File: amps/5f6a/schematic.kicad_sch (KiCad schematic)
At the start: 60 parts, among them T3 2R sec

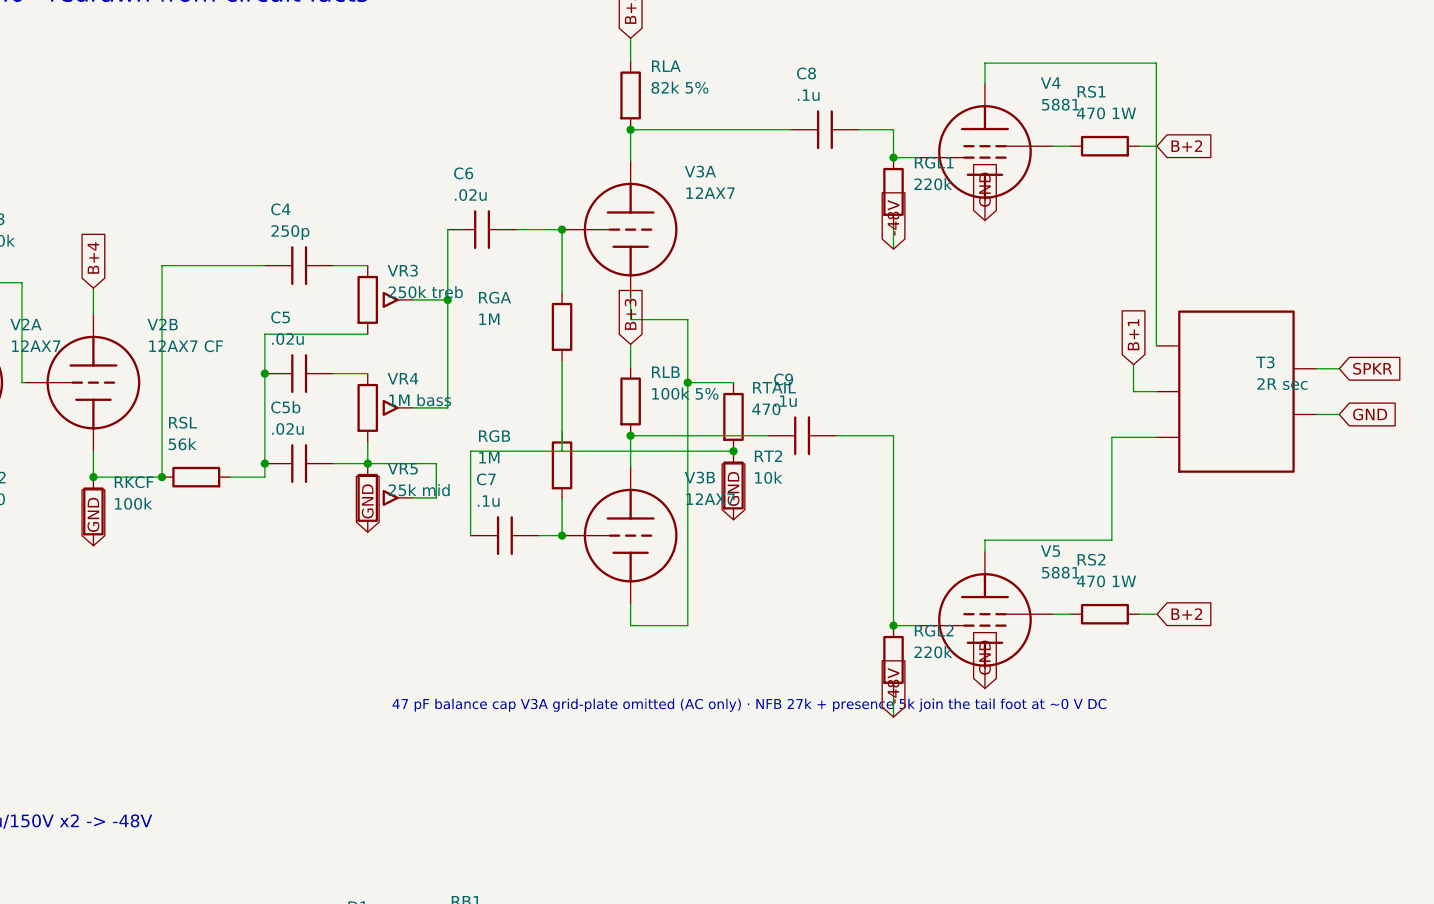
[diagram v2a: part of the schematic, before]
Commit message: Fix: the 5F6-A, AB763 and AA1164 draw the ladder their own sheets print
The tone-stack audit (dc65fcf) flagged these schematics as still drawing
the "canonical FMV" joined network. Fetching each amp's published drawing
and reading it at lug level (300-400 dpi crops) settles all three:

- Fender 5F6-A (I-EG), schematic AND factory layout: the same ladder as
  the 5F6 — 250 pF and the 56k slope both leave the cathode-follower
  node; the first 0.02 uF lands on the node shared by the treble pot's
  LOWER lug and the bass pot; the bass pot is a rheostat (the layout
  sheet straps its wiper into the treble-lug node); the second 0.02 uF
  feeds the MIDDLE POT'S WIPER; the output is the treble wiper alone.
  Unlike the 5F6, the middle pot's foot grounds directly — the presence
  control lives at the phase-inverter tail, as already drawn.

- Fender AB763 (C-FD): BOTH channels print the AA964's two-knob ladder,
  part for part. The vibrato channel's drawn stack was wrong beyond the
  wiring: it was missing its 100k slope and its 0.1/0.047 capacitors
  outright (the 6.8k bleed stood in as a "slope"), and its 47 pF bright
  cap sits across the VOLUME pot (top lug to wiper), not the treble pot.
  The missing parts join bom.yaml (RSV, CBV, CBV2) and the schematic.

- Fender AA1164 (D 045427 rev A): the same two-knob ladder — treble
  lower lug on the far side of the 0.1 uF, bass rheostat above the
  0.047/6.8k foot, treble-wiper output.

The three lab presets now declare `wiring: 'ladder'` and
check_tonestack_wiring asserts the drawn node set for each. All 18
schematics round-trip; the wiring gate reports 9/9.

Co-Authored-By: Claude Fable 5 <noreply@anthropic.com>
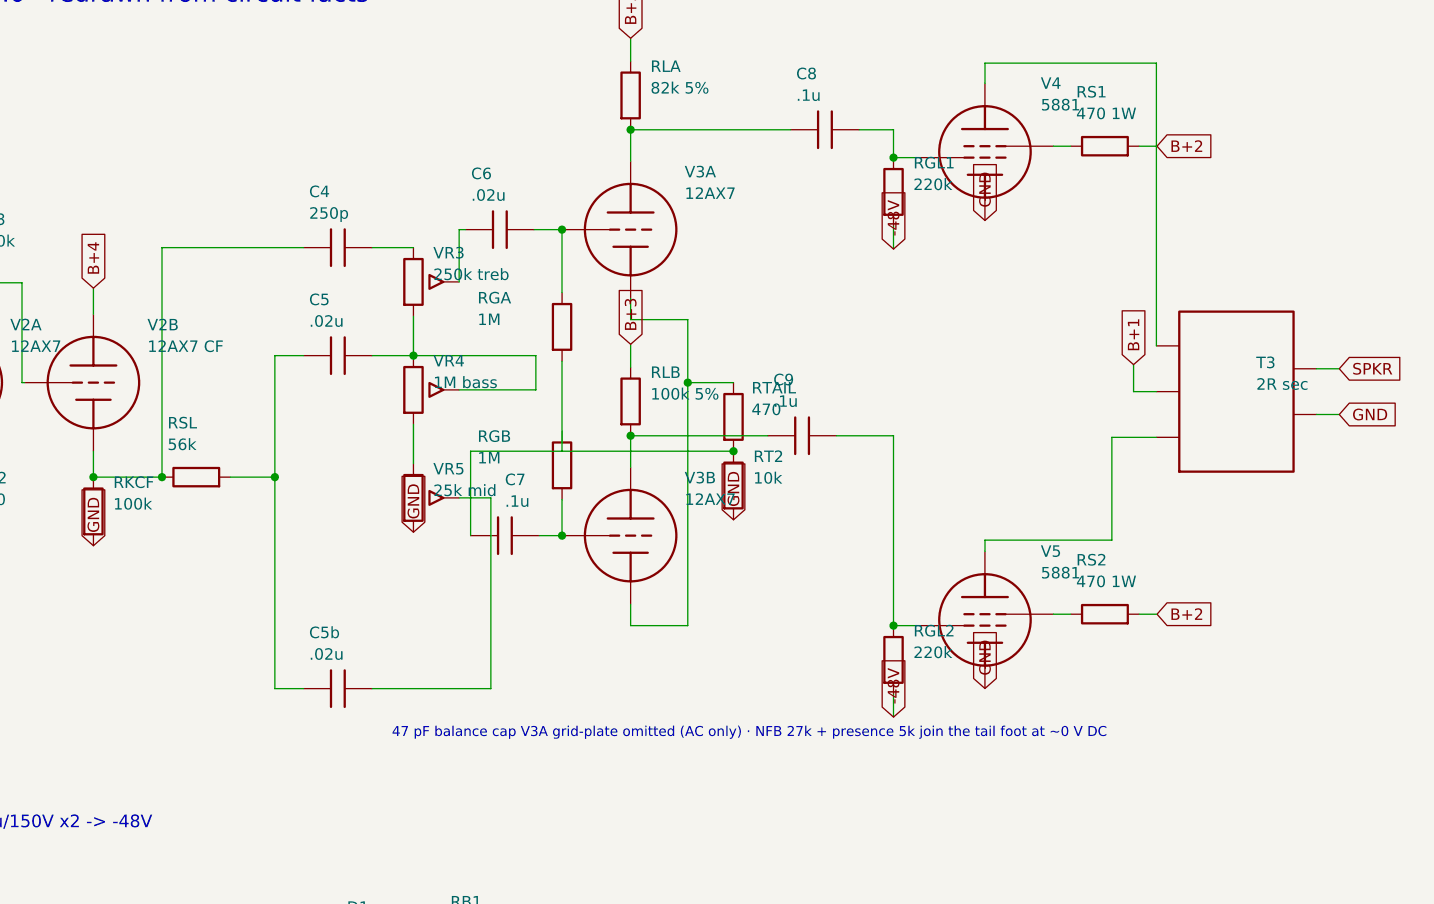
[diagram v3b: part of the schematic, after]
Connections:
- net at C6.1, VR3.2 (W): no longer VR4.2 (W)
- net at C5.1, C5b.1, RSL.2: no longer VR3.3
- net at C5.2, VR4.1: now also VR3.3, VR4.2 (W)
- net at C5b.2, VR5.2 (W): no longer VR4.3, VR5.1
- new net: VR4.3, VR5.1
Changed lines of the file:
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@@
     (stroke (width 0) (type default)))
   (junction (at 124.46 119.5) (diameter 0) (color 0 0 0 0))
-  (wire (pts (xy 124.46 119.5) (xy 124.46 96))
+  (wire (pts (xy 124.46 119.5) (xy 124.46 94))
     (stroke (width 0) (type default)))
-  (wire (pts (xy 124.46 96) (xy 135.89 96))
+  (wire (pts (xy 124.46 94) (xy 140.19 94))
     (stroke (width 0) (type default)))
   (symbol (lib_id "cx:R") (at 128.27 119.5 90) (unit 1)
@@
     (property "Reference" "RSL" (at 125.07 113.5 270) (effects (font (size 1.27 1.27)) (justify left)))
     (property "Value" "56k" (at 125.07 115.9 270) (effects (font (size 1.27 1.27)) (justify left))))
-  (wire (pts (xy 132.08 119.5) (xy 135.89 119.5))
+  (wire (pts (xy 132.08 119.5) (xy 137 119.5))
     (stroke (width 0) (type default)))
-  (wire (pts (xy 135.89 119.5) (xy 135.89 103.62))
+  (symbol (lib_id "cx:C") (at 144 94 90) (unit 1)
+    (in_bom yes) (on_board yes)
+    (property "Reference" "C4" (at 140.8 87.8 270) (effects (font (size 1.27 1.27)) (justify left)))
+    (property "Value" "250p" (at 140.8 90.2 270) (effects (font (size 1.27 1.27)) (justify left))))
+  (wire (pts (xy 147.81 94) (xy 152.4 94))
     (stroke (width 0) (type default)))
-  (wire (pts (xy 135.89 103.62) (xy 147.32 103.62))
+  (symbol (lib_id "cx:POT") (at 152.4 97.81 0) (unit 1)
+    (in_bom yes) (on_board yes)
+    (property "Reference" "VR3" (at 154.6 94.61 0) (effects (font (size 1.27 1.27)) (justify left)))
+    (property "Value" "250k treb" (at 154.6 97.01 0) (effects (font (size 1.27 1.27)) (justify left))))
+  (junction (at 137 119.5) (diameter 0) (color 0 0 0 0))
+  (wire (pts (xy 137 119.5) (xy 137 106))
     (stroke (width 0) (type default)))
-  (junction (at 135.89 108) (diameter 0) (color 0 0 0 0))
-  (junction (at 135.89 118) (diameter 0) (color 0 0 0 0))
-  (symbol (lib_id "cx:C") (at 139.7 96 90) (unit 1)
+  (symbol (lib_id "cx:C") (at 144 106 90) (unit 1)
     (in_bom yes) (on_board yes)
-    (property "Reference" "C4" (at 136.5 89.8 270) (effects (font (size 1.27 1.27)) (justify left)))
-    (property "Value" "250p" (at 136.5 92.2 270) (effects (font (size 1.27 1.27)) (justify left))))
-  (wire (pts (xy 143.51 96) (xy 147.32 96))
+    (property "Reference" "C5" (at 140.8 99.8 270) (effects (font (size 1.27 1.27)) (justify left)))
+    (property "Value" ".02u" (at 140.8 102.2 270) (effects (font (size 1.27 1.27)) (justify left))))
+  (wire (pts (xy 137 106) (xy 140.19 106))
     (stroke (width 0) (type default)))
-  (symbol (lib_id "cx:POT") (at 147.32 99.81 0) (unit 1)
+  (wire (pts (xy 147.81 106) (xy 152.4 106))
+    (stroke (width 0) (type default)))
+  (wire (pts (xy 137 119.5) (xy 137 143))
+    (stroke (width 0) (type default)))
+  (symbol (lib_id "cx:C") (at 144 143 90) (unit 1)
     (in_bom yes) (on_board yes)
-    (property "Reference" "VR3" (at 149.52 96.61 0) (effects (font (size 1.27 1.27)) (justify left)))
-    (property "Value" "250k treb" (at 149.52 99.01 0) (effects (font (size 1.27 1.27)) (justify left))))
-  (symbol (lib_id "cx:C") (at 139.7 108 90) (unit 1)
+    (property "Reference" "C5b" (at 140.8 136.8 270) (effects (font (size 1.27 1.27)) (justify left)))
+    (property "Value" ".02u" (at 140.8 139.2 270) (effects (font (size 1.27 1.27)) (justify left))))
+  (wire (pts (xy 137 143) (xy 140.19 143))
+    (stroke (width 0) (type default)))
+  (wire (pts (xy 147.81 143) (xy 161 143))
+    (stroke (width 0) (type default)))
+  (wire (pts (xy 161 143) (xy 161 121.81))
+    (stroke (width 0) (type default)))
+  (wire (pts (xy 161 121.81) (xy 157.48 121.81))
+    (stroke (width 0) (type default)))
+  (wire (pts (xy 152.4 101.62) (xy 152.4 106))
+    (stroke (width 0) (type default)))
+  (symbol (lib_id "cx:POT") (at 152.4 109.81 0) (unit 1)
     (in_bom yes) (on_board yes)
-    (property "Reference" "C5" (at 136.5 101.8 270) (effects (font (size 1.27 1.27)) (justify left)))
-    (property "Value" ".02u" (at 136.5 104.2 270) (effects (font (size 1.27 1.27)) (justify left))))
-  (wire (pts (xy 143.51 108) (xy 147.32 108))
+    (property "Reference" "VR4" (at 154.6 106.61 0) (effects (font (size 1.27 1.27)) (justify left)))
+    (property "Value" "1M bass" (at 154.6 109.01 0) (effects (font (size 1.27 1.27)) (justify left))))
+  (wire (pts (xy 157.48 109.81) (xy 166 109.81))
     (stroke (width 0) (type default)))
-  (symbol (lib_id "cx:POT") (at 147.32 111.81 0) (unit 1)
+  (wire (pts (xy 166 109.81) (xy 166 106))
+    (stroke (width 0) (type default)))
+  (wire (pts (xy 166 106) (xy 152.4 106))
+    (stroke (width 0) (type default)))
+  (junction (at 152.4 106) (diameter 0) (color 0 0 0 0))
+  (wire (pts (xy 152.4 113.62) (xy 152.4 118))
+    (stroke (width 0) (type default)))
+  (symbol (lib_id "cx:POT") (at 152.4 121.81 0) (unit 1)
     (in_bom yes) (on_board yes)
-    (property "Reference" "VR4" (at 149.52 108.61 0) (effects (font (size 1.27 1.27)) (justify left)))
-    (property "Value" "1M bass" (at 149.52 111.01 0) (effects (font (size 1.27 1.27)) (justify left))))
-  (symbol (lib_id "cx:C") (at 139.7 118 90) (unit 1)
+    (property "Reference" "VR5" (at 154.6 118.61 0) (effects (font (size 1.27 1.27)) (justify left)))
+    (property "Value" "25k mid" (at 154.6 121.01 0) (effects (font (size 1.27 1.27)) (justify left))))
+  (global_label "GND" (shape input) (at 152.4 125.62 270)
+    (effects (font (size 1.27 1.27)) (justify left)))
+  (wire (pts (xy 157.48 97.81) (xy 157.48 92))
+    (stroke (width 0) (type default)))
+  (symbol (lib_id "cx:C") (at 162 92 90) (unit 1)
     (in_bom yes) (on_board yes)
-    (property "Reference" "C5b" (at 136.5 111.8 270) (effects (font (size 1.27 1.27)) (justify left)))
-    (property "Value" ".02u" (at 136.5 114.2 270) (effects (font (size 1.27 1.27)) (justify left))))
-  (wire (pts (xy 143.51 118) (xy 147.32 118))
+    (property "Reference" "C6" (at 158.8 85.8 270) (effects (font (size 1.27 1.27)) (justify left)))
+    (property "Value" ".02u" (at 158.8 88.2 270) (effects (font (size 1.27 1.27)) (justify left))))
+  (wire (pts (xy 157.48 92) (xy 158.19 92))
     (stroke (width 0) (type default)))
-  (wire (pts (xy 147.32 115.62) (xy 147.32 118))
-    (stroke (width 0) (type default)))
-  (symbol (lib_id "cx:POT") (at 147.32 121.81 0) (unit 1)
-    (in_bom yes) (on_board yes)
-    (property "Reference" "VR5" (at 149.52 118.61 0) (effects (font (size 1.27 1.27)) (justify left)))
-    (property "Value" "25k mid" (at 149.52 121.01 0) (effects (font (size 1.27 1.27)) (justify left))))
-  (global_label "GND" (shape input) (at 147.32 125.62 270)
-    (effects (font (size 1.27 1.27)) (justify left)))
-  (wire (pts (xy 152.4 121.81) (xy 154.94 121.81))
-    (stroke (width 0) (type default)))
-  (wire (pts (xy 154.94 121.81) (xy 154.94 118))
-    (stroke (width 0) (type default)))
-  (wire (pts (xy 154.94 118) (xy 147.32 118))
-    (stroke (width 0) (type default)))
-  (junction (at 147.32 118) (diameter 0) (color 0 0 0 0))
-  (wire (pts (xy 152.4 99.81) (xy 156.21 99.81))
-    (stroke (width 0) (type default)))
-  (wire (pts (xy 152.4 111.81) (xy 156.21 111.81))
-    (stroke (width 0) (type default)))
-  (wire (pts (xy 156.21 111.81) (xy 156.21 99.81))
-    (stroke (width 0) (type default)))
-  (junction (at 156.21 99.81) (diameter 0) (color 0 0 0 0))
-  (wire (pts (xy 156.21 99.81) (xy 156.21 92))
-    (stroke (width 0) (type default)))
-  (symbol (lib_id "cx:C") (at 160.02 92 90) (unit 1)
-    (in_bom yes) (on_board yes)
-    (property "Reference" "C6" (at 156.82 85.8 270) (effects (font (size 1.27 1.27)) (justify left)))
-    (property "Value" ".02u" (at 156.82 88.2 270) (effects (font (size 1.27 1.27)) (justify left))))
-  (wire (pts (xy 163.83 92) (xy 168.91 92))
+  (wire (pts (xy 165.81 92) (xy 168.91 92))
     (stroke (width 0) (type default)))
   (symbol (lib_id "cx:TRIODE") (at 176.53 92 0) (unit 1)
@@
   (symbol (lib_id "cx:C") (at 162.56 126 90) (unit 1)
     (in_bom yes) (on_board yes)
-    (property "Reference" "C7" (at 159.36 119.8 270) (effects (font (size 1.27 1.27)) (justify left)))
-    (property "Value" ".1u" (at 159.36 122.2 270) (effects (font (size 1.27 1.27)) (justify left))))
+    (property "Reference" "C7" (at 162.56 119.8 270) (effects (font (size 1.27 1.27)) (justify left)))
+    (property "Value" ".1u" (at 162.56 122.2 270) (effects (font (size 1.27 1.27)) (justify left))))
   (wire (pts (xy 166.37 126) (xy 168.91 126))
     (stroke (width 0) (type default)))
@@
   (wire (pts (xy 158.75 116.62) (xy 168.91 116.62))
     (stroke (width 0) (type default)))
-  (text "47 pF balance cap V3A grid-plate omitted (AC only) · NFB 27k + presence 5k join the tail foot at ~0 V DC" (at 150 145 0)
+  (text "47 pF balance cap V3A grid-plate omitted (AC only) · NFB 27k + presence 5k join the tail foot at ~0 V DC" (at 150 148 0)
     (effects (font (size 1.1 1.1)) (justify left)))
   (wire (pts (xy 176.53 80.9) (xy 194.31 80.9))
